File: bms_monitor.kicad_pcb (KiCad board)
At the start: 2 copper layers, 115 x 65 mm, 246 parts, among them CN1 10nF, CN10 10nF, CN11 10nF, CN12 10nF, CN13 10nF, CN14 10nF, CN2 10nF, CN3 10nF, CN4 10nF, CN5 10nF, CN6 10nF, CN7 10nF, CN8 10nF, CN9 10nF, J1 Conn_01x02, J10 TEMP0, J11 TEMP1, J12 Conn_01x05, J14 5V, J15 Conn_ST_STDC14, J2 Conn_01x02, J3 Conn_01x02, J4 Conn_01x02, J5 CELLS, J6 TEMP0, J7 TEMP1, J8 Conn_01x05, J9 CELLS, Q1 NSV1C201MZ4, Q2 NSV1C201MZ4, Q3 PMV65XP, U1 STM32L432KBUx, U10 CD74HC4067SM, U11 MP4541, U12 SM91502ALA, U13 SM91502ALA, U14 SM91502ALA, U3 DSC61XX, U4 TFBS4652, U5 LTC6811-1, U6 CD74HC4067SM, U7 MP4541, U8 SM91502ALA, U9 LTC6811-1

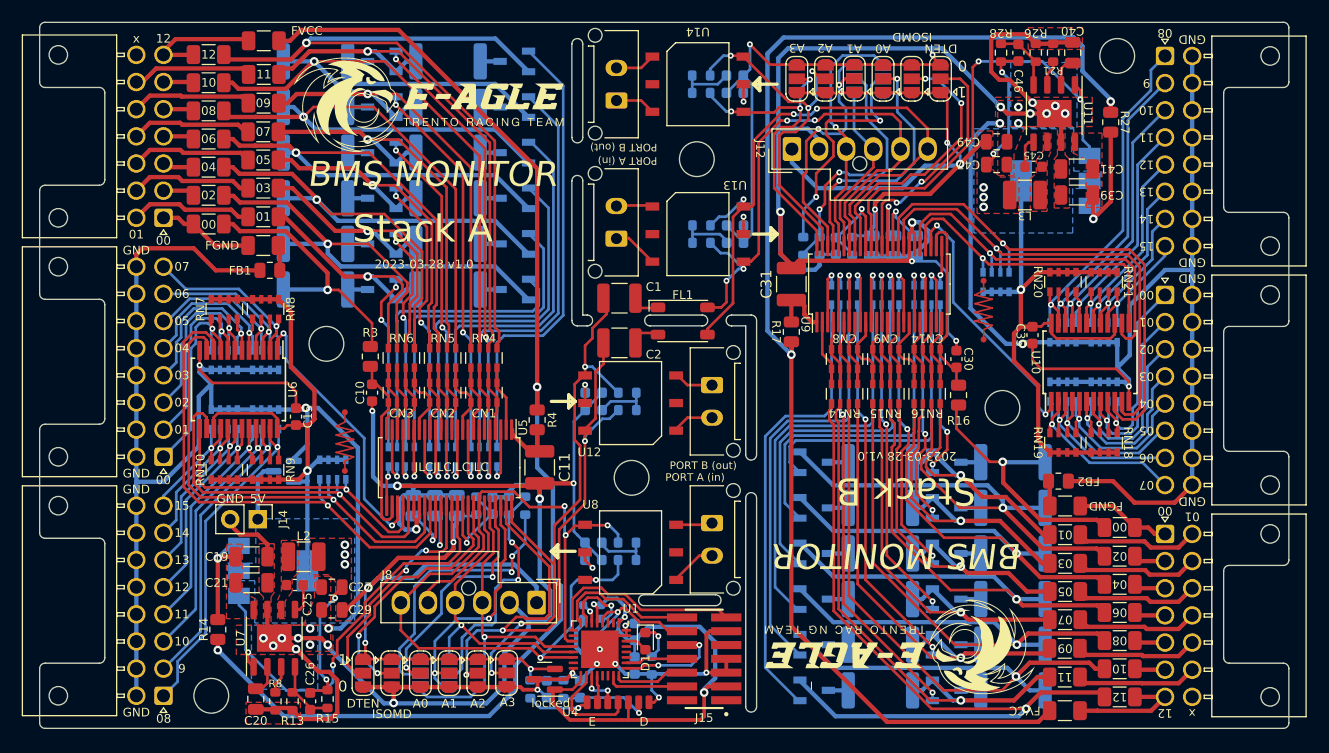
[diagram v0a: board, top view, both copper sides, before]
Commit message: fix
- Changed oscillator footprint
- tied mux enable to ground
- Corrected power BJT's footprint
- added 5V presence led
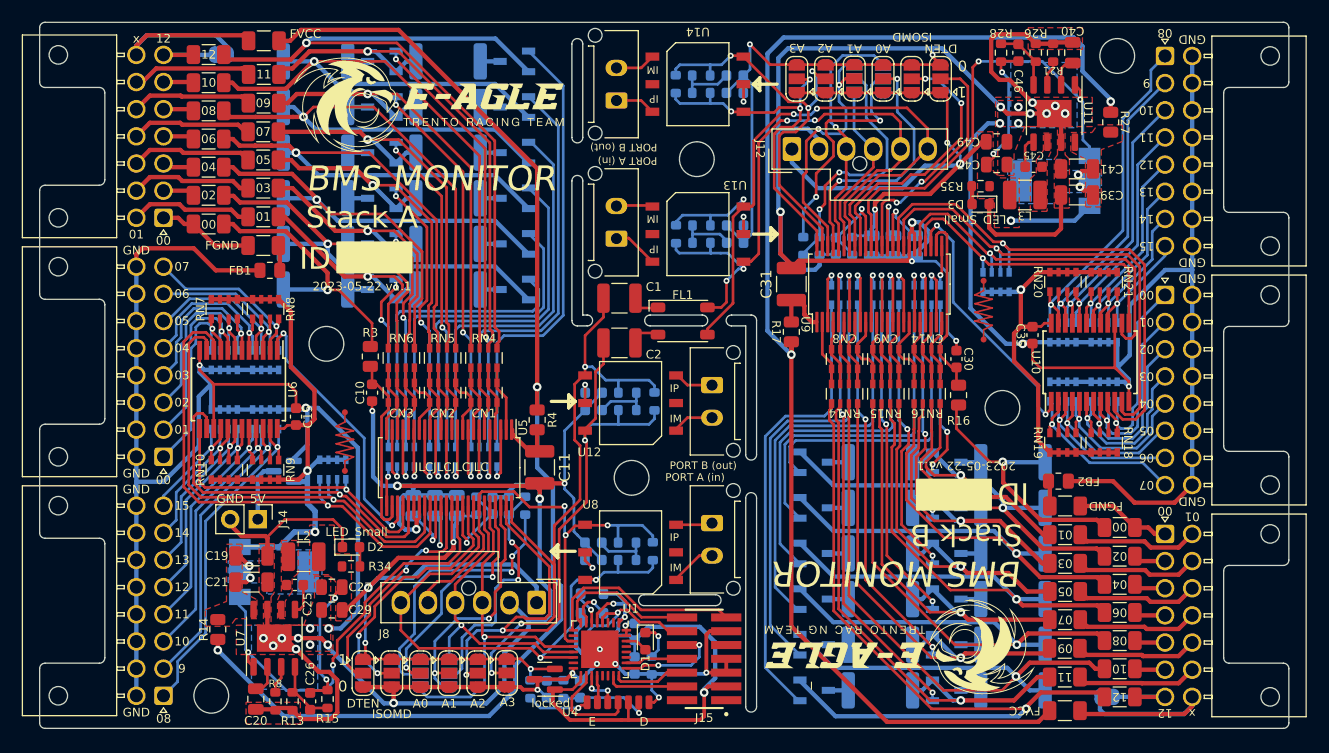
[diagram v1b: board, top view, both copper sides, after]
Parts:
- added D2: LED_Small, LED_SMD:LED_0603_1608Metric, F.Cu at (108.7, 110.3)
- added D3: LED_Small, LED_SMD:LED_0603_1608Metric, F.Cu at (166.6, 78.7)
- added JP17: isoIP, Jumper:SolderJumper-2_P1.3mm_Open_RoundedPad1.0x1.5mm, B.Cu at (96.7, 65.0)
- added JP18: isoIP, Jumper:SolderJumper-2_P1.3mm_Open_RoundedPad1.0x1.5mm, B.Cu at (178.3, 124.1)
- added R30: 100, Resistor_SMD:R_0603_1608Metric, B.Cu at (136.4, 110.7)
- added R31: 100, Resistor_SMD:R_0603_1608Metric, B.Cu at (136.6, 96.9)
- added R32: 100, Resistor_SMD:R_0603_1608Metric, B.Cu at (138.6, 81.5)
- added R33: 100, Resistor_SMD:R_0603_1608Metric, B.Cu at (138.6, 67.7)
- added R34: 1K, Resistor_SMD:R_0603_1608Metric, F.Cu at (108.7, 112.1)
- added R35: 1K, Resistor_SMD:R_0603_1608Metric, F.Cu at (166.6, 77.1)
- CN10, CN11, CN12, CN13, CN4, CN5, CN6, CN7: value 10nF -> 100nF
- Q1, Q2: value NSV1C201MZ4 -> NSS1C201MZ4; footprint Package_TO_SOT_SMD:SOT-223-3_TabPin2 -> Package_TO_SOT_SMD:SOT-223
- RN10, RN18, RN19, RN20, RN21, RN7, RN8, RN9: value 100R -> 27K
- U10, U6: value CD74HC4067SM -> 74HC4067PW,118
- moved U3 0.80 mm to (130.6, 115.5)
- moved Q1 0.12 mm to (101.6, 112.6)
- moved C19 0.08 mm to (99.5, 111.1)
- moved C21 0.06 mm to (99.5, 113.5)
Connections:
- Fa13 pad 2: Net-(Fa12-Pad2) -> Net-(Fa13-Pad2)
- Fb3 pad 2: Net-(F13-Pad2) -> Net-(Fb3-Pad2)
- J5 pad 14: unconnected-(J5-Pad14) -> Net-(Fa13-Pad2)
- J9 pad 14: unconnected-(J9-Pad14) -> Net-(Fb3-Pad2)
- Q1 pad 2: +5V -> /StackA/PSU_INPUT
- Q1 pad 3: /StackA/PSU_INPUT -> +5V
- Q2 pad 2: /StackB/VCC -> /StackB/PSU_INPUT
- Q2 pad 3: /StackB/PSU_INPUT -> /StackB/VCC
- U10 pad 15: /StackB/VCC -> /StackB/GND
- U6 pad 15: +5V -> GND
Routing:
- net Net-(Fa13-Pad2): track 0.00 -> 22.6 mm
- net Net-(Fb3-Pad2): track 0.00 -> 22.2 mm
- net /StackB/GND: track 288.1 -> 303.9 mm
- net GND: track 329.8 -> 344.0 mm
- net /StackB/VCC: track 129.2 -> 118.9 mm, vias 9 -> 7
- net /StackB/PSU_INPUT: track 11.7 -> 4.14 mm, vias 1 -> 2
- net /StackA/PSU_INPUT: track 9.43 -> 3.02 mm, vias 1 -> 2
- net /StackA/A2: track 62.2 -> 67.5 mm
- net /IA+_A: track 40.9 -> 45.6 mm
- net /IB+_B: track 29.1 -> 33.7 mm
- net /StackA/A3: track 55.6 -> 60.1 mm
- net /StackB/IA+: track 51.5 -> 56.0 mm
- net /StackB/CSB: track 58.0 -> 62.3 mm
- net Net-(Fa12-Pad2): track 11.5 -> 7.40 mm
- net /CS: track 47.7 -> 51.7 mm
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- added copper zone on B.Cu, net /StackA/PSU_INPUT
- added copper zone on B.Cu, net /StackB/PSU_INPUT
- removed copper zone on B.Cu, net +5V
- removed copper zone on B.Cu, net /StackB/VCC
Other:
- board text added: "2023-05-22 v1.1"
- board text added: "ID"
- board text added: "IM"
- board text added: "IP"
- board text added: "VDD"
- board text removed: "2023-03-28 v1.0"
- board text removed: "PSU_INPUT"
